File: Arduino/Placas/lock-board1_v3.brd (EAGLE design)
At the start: 87.5 x 106.5 mm, 9 parts

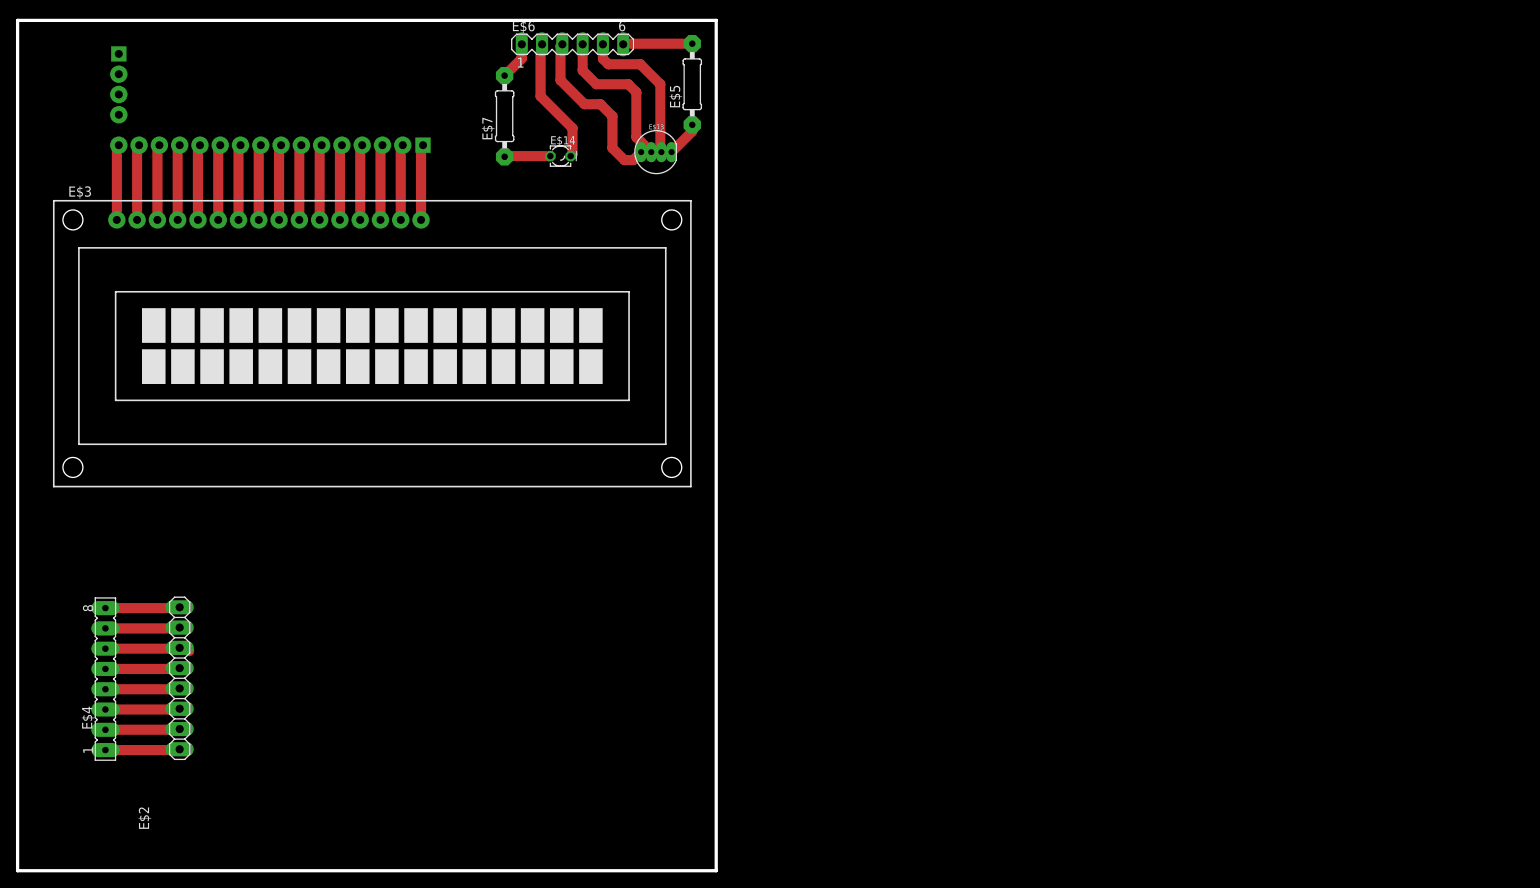
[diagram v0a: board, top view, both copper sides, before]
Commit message: board v3 created, not tested
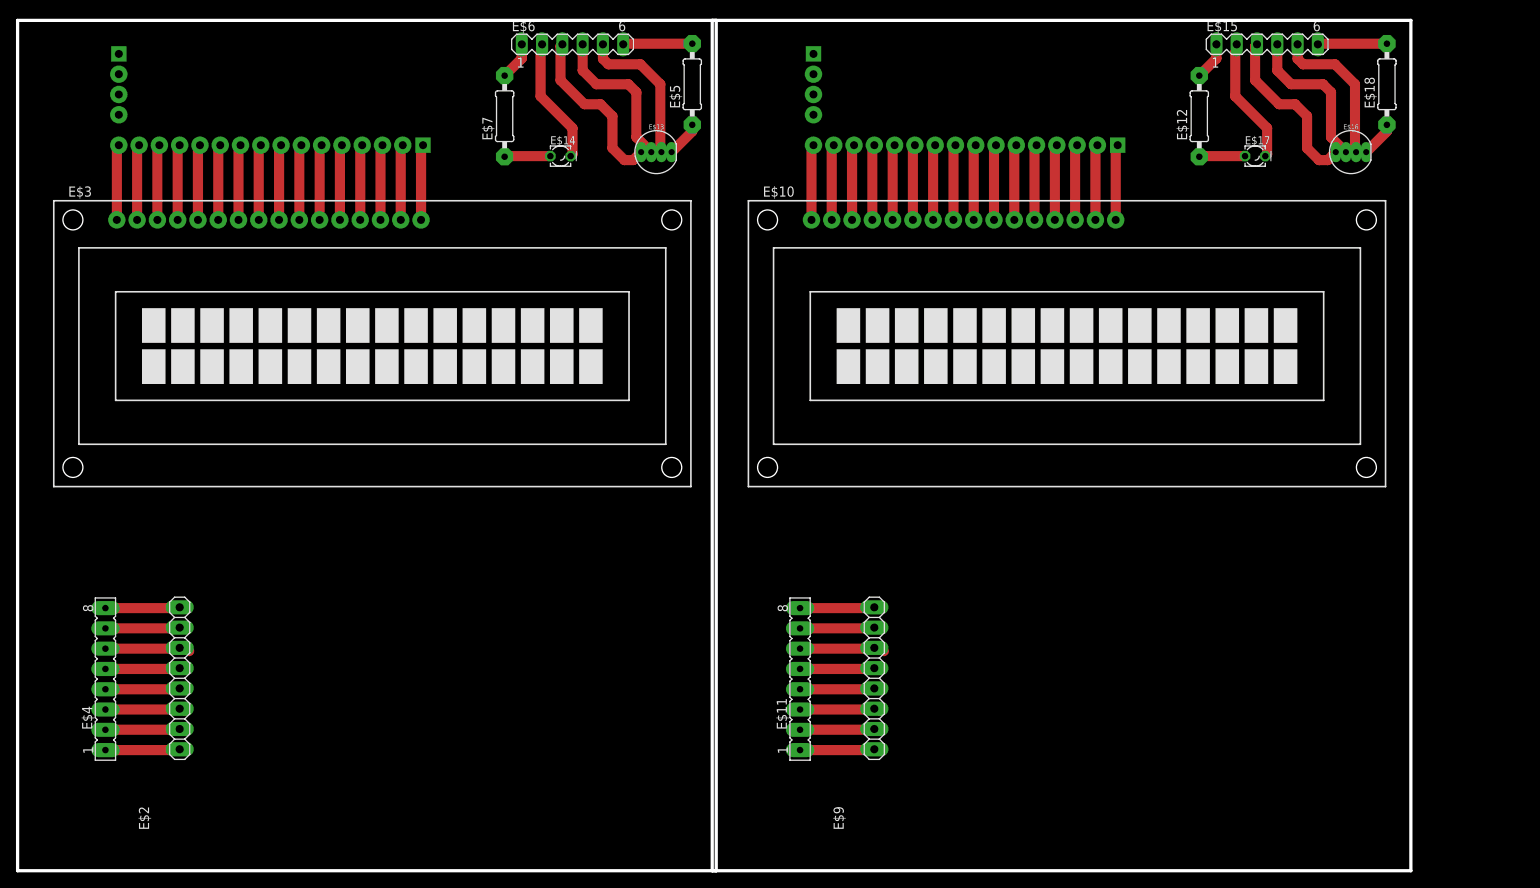
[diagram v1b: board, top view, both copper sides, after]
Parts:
- added E$10: (no value), display-lcd:TUXGR_16X2_R2
- added E$11: (no value), con-lsta:FE08
- added E$12, E$18: (no value), eagle-ltspice:0207/10
- added E$15: (no value), con-lstb:MA06-1
- added E$16: (no value), SparkFun-LED:LED-RGB-THRU
- added E$17: (no value), eagle-ltspice:LED_LD260
- added E$8: (no value), converter_lcd_serial_i2c:LCD-I2C-CONVERTER
- added E$9: (no value), mfrc522-module:RFID-RC522
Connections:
- new net S$34: E$10.1, E$8.J2.16
- new net S$35: E$10.2, E$8.J2.15
- new net S$36: E$10.3, E$8.J2.14
- new net S$37: E$10.4, E$8.J2.13
- new net S$38: E$10.5, E$8.J2.12
- new net S$39: E$10.6, E$8.J2.11
- new net S$40: E$10.7, E$8.J2.10
- new net S$41: E$10.8, E$8.J2.9
- new net S$42: E$10.9, E$8.J2.8
- new net S$43: E$10.10, E$8.J2.7
- new net S$44: E$10.11, E$8.J2.6
- new net S$45: E$10.13, E$8.J2.4
- new net S$46: E$10.14, E$8.J2.3
- new net S$47: E$10.15, E$8.J2.2
- new net S$48: E$10.16, E$8.J2.1
- new net S$49: E$10.12, E$8.J2.5
- new net S$50: E$11.8, E$9.SS
- new net S$51: E$11.7, E$9.SCK
- new net S$52: E$11.6, E$9.MOSI
- new net S$53: E$11.5, E$9.MISO
- new net S$54: E$9.IRQ
- new net S$55: E$11.4
- new net S$56: E$11.3, E$9.GND
- new net S$57: E$11.2, E$9.RST
- new net S$58: E$11.1, E$9.3V3
- new net S$59: E$12.1, E$17.A
- new net S$60: E$15.6, E$18.2
- new net S$61: E$12.2, E$15.1
- new net S$62: E$16.1, E$18.1
- new net S$63: E$15.5, E$16.2
- new net S$64: E$15.4, E$16.3
- new net S$65: E$15.3, E$16.4
- new net S$66: E$15.2, E$17.K
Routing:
- net S$65: track 0.00 -> 21.6 mm
- net S$64: track 0.00 -> 19.4 mm
- net S$63: track 0.00 -> 18.9 mm
- net S$66: track 0.00 -> 15.8 mm
- net S$52: track 0.00 -> 10.6 mm
- net S$56: track 0.00 -> 10.1 mm
- net S$57: track 0.00 -> 10.1 mm
- net S$51: track 0.00 -> 10.1 mm
- net S$58: track 0.00 -> 10.0 mm
- net S$50: track 0.00 -> 10.0 mm
- net S$49: track 0.00 -> 9.46 mm
- net S$48: track 0.00 -> 9.46 mm
- net S$47: track 0.00 -> 9.46 mm
- net S$46: track 0.00 -> 9.46 mm
- net S$45: track 0.00 -> 9.46 mm
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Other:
- board size 87.5 x 106.5 mm -> 174.5 x 106.5 mm

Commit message: Lock board updated
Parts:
- removed E$10: (no value), display-lcd:TUXGR_16X2_R2
- removed E$12: (no value), eagle-ltspice:0207/10
- removed E$13, E$16: (no value), SparkFun-LED:LED-RGB-THRU
- removed E$14, E$17: (no value), eagle-ltspice:LED_LD260
- removed E$15, E$6: (no value), con-lstb:MA06-1
- removed E$8: (no value), converter_lcd_serial_i2c:LCD-I2C-CONVERTER
- E$1: device converter_lcd_serial_i2c:LCD-I2C-CONVERTER -> SparkFun-LED:LED-RGB-THRU
- E$2: device mfrc522-module:RFID-RC522 -> SparkFun-LED:LED-RGB-THRU
- E$3: device display-lcd:TUXGR_16X2_R2 -> eagle-ltspice:0207/10
- E$4: device con-lsta:FE08 -> con-lstb:MA07-1
- E$5: device eagle-ltspice:0207/10 -> buzzer:AL60P
- moved E$4 156.5 mm to (198.0, 38.0)
- moved E$1 155.7 mm to (205.0, 49.0), flipped to the top, turned to 90 degrees
- moved E$2 154.3 mm to (205.0, 33.0)
- moved E$7 131.1 mm to (211.0, 54.5), turned to 180 degrees
- moved E$3 126.4 mm to (187.0, 21.5), turned to 180 degrees
- moved E$5 111.7 mm to (213.0, 59.0), turned to 0 degrees
- moved E$18 87.3 mm to (187.0, 26.5), turned to 180 degrees
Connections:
- removed net S$14: E$1.J2.2, E$3.15
- removed net S$15: E$1.J2.1, E$3.16
- removed net S$16: E$1.J2.5, E$3.12
- removed net S$17: E$2.SS, E$4.8
- removed net S$18: E$2.SCK, E$4.7
- removed net S$19: E$2.MOSI, E$4.6
- removed net S$2: E$1.J2.15, E$3.2
- removed net S$20: E$2.MISO, E$4.5
- removed net S$21: E$4.4
- removed net S$22: E$2.GND, E$4.3
- removed net S$23: E$2.RST, E$4.2
- removed net S$24: E$2.3V3, E$4.1
- removed net S$25: E$2.IRQ
- removed net S$26: E$1.J2.6, E$3.11
- removed net S$27: E$6.1, E$7.2
- removed net S$28: E$5.2, E$6.6
- removed net S$29: E$13.1, E$5.1
- removed net S$30: E$13.2, E$6.5
- removed net S$31: E$13.3, E$6.4
- removed net S$32: E$13.4, E$6.3
- removed net S$33: E$14.K, E$6.2
- removed net S$34: E$10.1, E$8.J2.16
- removed net S$35: E$10.2, E$8.J2.15
- removed net S$36: E$10.3, E$8.J2.14
- removed net S$37: E$10.4, E$8.J2.13
- removed net S$38: E$10.5, E$8.J2.12
- removed net S$39: E$10.6, E$8.J2.11
- removed net S$40: E$10.7, E$8.J2.10
- removed net S$41: E$10.8, E$8.J2.9
- removed net S$42: E$10.9, E$8.J2.8
- removed net S$43: E$10.10, E$8.J2.7
- removed net S$44: E$10.11, E$8.J2.6
- removed net S$45: E$10.13, E$8.J2.4
- removed net S$46: E$10.14, E$8.J2.3
- removed net S$47: E$10.15, E$8.J2.2
- removed net S$48: E$10.16, E$8.J2.1
- removed net S$49: E$10.12, E$8.J2.5
- removed net S$5: E$1.J2.12, E$3.5
- removed net S$59: E$12.1, E$17.A
- removed net S$60: E$15.6, E$18.2
- removed net S$61: E$12.2, E$15.1
- removed net S$62: E$16.1, E$18.1
- removed net S$63: E$15.5, E$16.2
- removed net S$64: E$15.4, E$16.3
- removed net S$65: E$15.3, E$16.4
- removed net S$66: E$15.2, E$17.K
- removed net S$9: E$1.J2.8, E$3.9
- net S$1: now also E$18.1, E$2.3; no longer E$1.J2.16, E$3.1
- net S$10: now also E$2.1, E$4.3; no longer E$1.J2.7, E$3.10
- net S$11: now also E$1.4, E$4.4; no longer E$14.A, E$7.1
- net S$12: now also E$1.2, E$4.5; no longer E$1.J2.4, E$3.13
- net S$13: now also E$1.1, E$4.6; no longer E$1.J2.3, E$3.14
- net S$3: now also E$1.3, E$3.1; no longer E$1.J2.14, E$3.3
- net S$4: now also E$2.4, E$4.1; no longer E$1.J2.13, E$3.4
- net S$52: no longer E$9.MOSI
- net S$56: now also E$18.2, E$3.2, E$5.1
- net S$6: now also E$4.7, E$7.2; no longer E$1.J2.11, E$3.6
- net S$7: now also E$5.2, E$7.1; no longer E$1.J2.10, E$3.7
- net S$8: now also E$2.2, E$4.2; no longer E$1.J2.9, E$3.8
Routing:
- net S$56: track 10.1 -> 107.9 mm
- net S$3: track 9.46 -> 49.2 mm
- net S$32: track 21.6 -> 0.00 mm
- net S$65: track 21.6 -> 0.00 mm
- net S$64: track 19.4 -> 0.00 mm
- net S$31: track 19.4 -> 0.00 mm
- net S$30: track 18.9 -> 0.00 mm
- net S$63: track 18.9 -> 0.00 mm
- net S$33: track 15.8 -> 0.00 mm
- net S$66: track 15.8 -> 0.00 mm
- net S$1: track 9.46 -> 25.1 mm
- net S$6: track 9.46 -> 22.2 mm
- net S$19: track 10.6 -> 0.00 mm
- net S$22: track 10.1 -> 0.00 mm
- net S$23: track 10.1 -> 0.00 mm
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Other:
- board outline removed
- board text added: "+ B"
- board text added: "110"
- board text added: "220"
- board text added: "R G B"
